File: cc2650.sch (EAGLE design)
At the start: 23 parts, among them IC4 CC2650MODAMOHR, J1 AMP FCI 10103594-0001LF, SW1 SPST_TACT-KMR2, SW2 SPST_TACT-KMR2, U402 TPS62237DRY

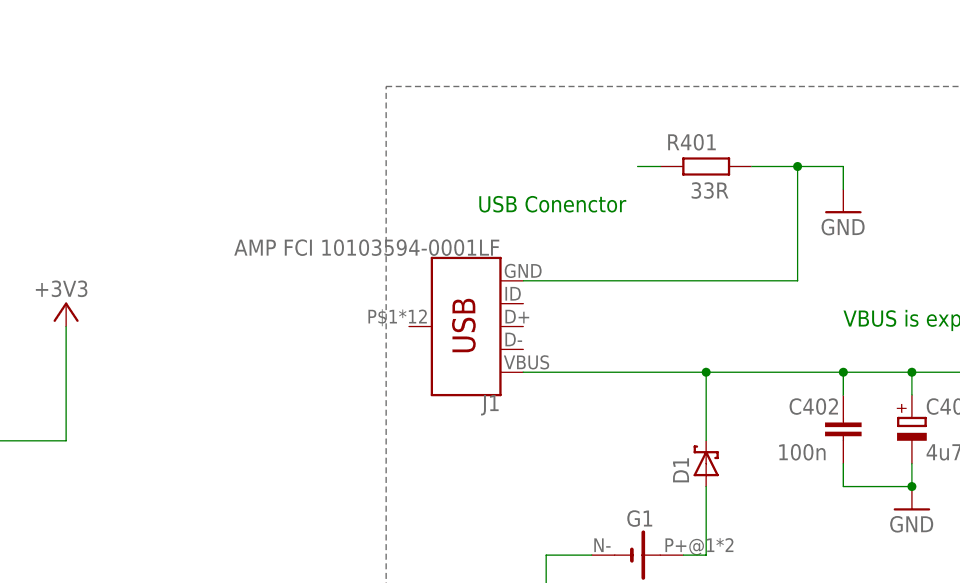
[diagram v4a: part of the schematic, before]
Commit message: Changed USB connector. Fixed error.
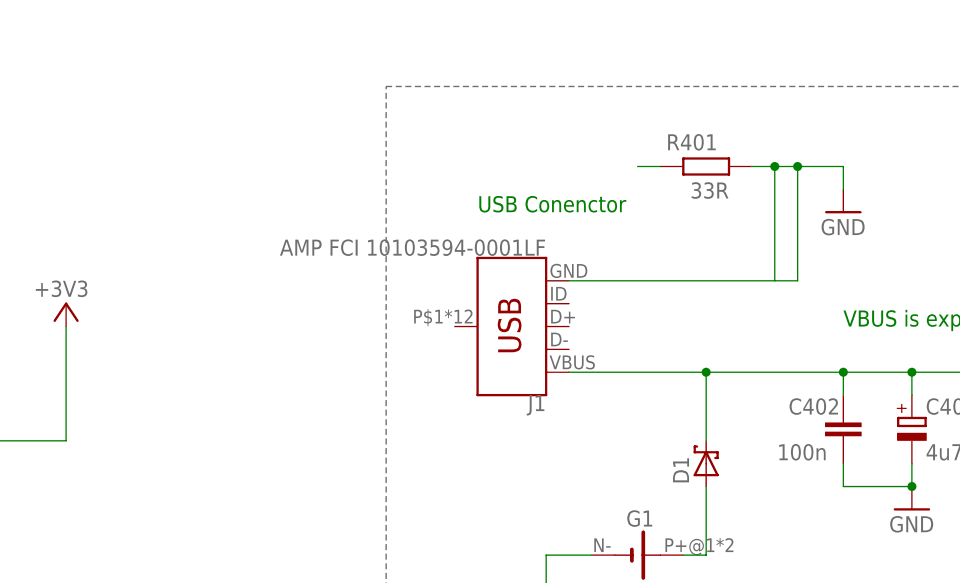
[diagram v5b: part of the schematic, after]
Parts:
- C17: MPN EVQ-Q2F03W -> (none); OC_NEWARK 96K9626 -> (none)
- C401, C402, C403, C404, D1, D2, G1, IC4, JP1, JP2, JP3, JP8, JTAG_CONNECTOR, L401, LED3, R27, R29, R401, SW1, SW2, U402: OC_NEWARK unknown -> (none)
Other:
- moved on the sheet: J1

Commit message: removed jumpers for power and leds.
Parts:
- removed JP1, JP8: LED1_PWR, jumper:JP1E
- U402: value TPS62237DRY -> TPS62233DRY
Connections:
- removed net N$7: JP8.2, R29.1
- new net PWR_LED_JMPR: JP3.4, R29.1
- net +3V3: now also JP3.2, JP3.3; no longer JP1.2, JP8.1
- net EZFET_VCC: now also JP3.1; no longer JP1.1
- net N$10: now also J1.SHIELD
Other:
- note added: "Use jumper on pins 1 & 2 for operation. Remove jumper to measure current."
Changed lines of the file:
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@@
 <part name="R29" library="rcl" deviceset="R-EU_" device="R0402" value="470R"/>
 <part name="GND21" library="supply1" deviceset="GND" device=""/>
-<part name="JP8" library="jumper" deviceset="JP1E" device="" value="LED1_PWR"/>
 <part name="LED3" library="led" deviceset="LED" device="CHIP-LED0603"/>
-<part name="+3V5" library="supply1" library_urn="urn:adsk.eagle:library:371" deviceset="+3V3" device=""/>
 <part name="GND56" library="supply1" deviceset="GND" device=""/>
 <part name="GND64" library="supply1" deviceset="GND" device=""/>
@@
 <part name="R401" library="rcl" deviceset="R-EU_" device="R0402" value="33R"/>
 <part name="C403" library="rcl" deviceset="CPOL-EU" device="A/3216-18R" value="4u7"/>
-<part name="JP1" library="jumper" deviceset="JP1E" device="" value="LED1_PWR"/>
-<part name="U402" library="tps62231dry" deviceset="TPS6223X_DRY_6" device="" value="TPS62237DRY"/>
+<part name="U402" library="tps62231dry" deviceset="TPS6223X_DRY_6" device="" value="TPS62233DRY"/>
 <part name="C404" library="CAP" deviceset="CSMD0805" device="" value="1u"/>
 <part name="C401" library="CAP" deviceset="CSMD0805" device="" value="1u"/>
@@
 <part name="GND54" library="supply1" deviceset="GND" device=""/>
 <part name="L401" library="MSP-EXP430F5659" deviceset="L-NR3010" device="" value="2.2uH (NR3010T2R2M)"/>
-<part name="+3V3" library="supply1" library_urn="urn:adsk.eagle:library:371" deviceset="+3V3" device=""/>
 <part name="D1" library="adafruit" deviceset="SCHOTTKY-DIODE" device="DO35-7"/>
 <part name="GND4" library="supply1" deviceset="GND" device=""/>
@@
 <wire x1="17.78" y1="-92.71" x2="127" y2="-92.71" width="0.1524" layer="95" style="shortdash"/>
 <text x="60.96" y="-45.72" size="1.778" layer="91">GPIO Programmable</text>
+<text x="-154.94" y="66.04" size="1.778" layer="91">Use jumper on pins 1 &amp; 2 for operation. Remove jumper to measure current.</text>
 </plain>
 <instances>
@@
 <attribute name="VALUE" x="45.72" y="83.82" size="1.778" layer="96"/>
 </instance>
-<instance part="+3V2" gate="G$1" x="-134.62" y="88.9" smashed="yes">
-<attribute name="VALUE" x="-132.08" y="91.44" size="1.778" layer="96" rot="R180"/>
+<instance part="+3V2" gate="G$1" x="-129.54" y="53.34" smashed="yes">
+<attribute name="VALUE" x="-127" y="55.88" size="1.778" layer="96" rot="R180"/>
 </instance>
 <instance part="R29" gate="G$1" x="129.54" y="68.58"/>
 <instance part="GND21" gate="1" x="154.94" y="60.96"/>
-<instance part="JP8" gate="A" x="116.84" y="71.12" smashed="yes">
-<attribute name="NAME" x="115.824" y="74.422" size="1.778" layer="95"/>
-</instance>
 <instance part="LED3" gate="G$1" x="139.7" y="68.58" rot="R90"/>
-<instance part="+3V5" gate="G$1" x="104.14" y="76.2" smashed="yes">
-<attribute name="VALUE" x="106.68" y="78.74" size="1.778" layer="96" rot="R180"/>
-</instance>
 <instance part="GND56" gate="1" x="68.58" y="17.78"/>
 <instance part="GND64" gate="1" x="76.2" y="-15.24"/>
@@
 <attribute name="NAME" x="77.724" y="-4.699" size="1.778" layer="95"/>
 <attribute name="VALUE" x="77.724" y="-9.779" size="1.778" layer="96"/>
-</instance>
-<instance part="JP1" gate="A" x="203.2" y="-7.62" smashed="yes">
-<attribute name="NAME" x="202.184" y="-4.318" size="1.778" layer="95"/>
 </instance>
 <instance part="U402" gate="&gt;NAME" x="142.24" y="-10.16"/>
@@
 <attribute name="NAME" x="160.02" y="8.89" size="1.778" layer="95" rot="R180"/>
 <attribute name="VALUE" x="170.18" y="3.81" size="1.778" layer="95" rot="R180"/>
-</instance>
-<instance part="+3V3" gate="G$1" x="213.36" y="0" smashed="yes">
-<attribute name="VALUE" x="215.9" y="2.54" size="1.778" layer="96" rot="R180"/>
 </instance>
 <instance part="D1" gate="G$1" x="53.34" y="-10.16" rot="R90"/>
@@
 <segment>
 <pinref part="+3V2" gate="G$1" pin="+3V3"/>
-<wire x1="-134.62" y1="83.82" x2="-134.62" y2="86.36" width="0.1524" layer="91"/>
-</segment>
-<segment>
-<pinref part="JP8" gate="A" pin="1"/>
-<wire x1="116.84" y1="68.58" x2="104.14" y2="68.58" width="0.1524" layer="91"/>
-<pinref part="+3V5" gate="G$1" pin="+3V3"/>
-<wire x1="104.14" y1="73.66" x2="104.14" y2="68.58" width="0.1524" layer="91"/>
-</segment>
-<segment>
-<pinref part="+3V3" gate="G$1" pin="+3V3"/>
-<wire x1="213.36" y1="-10.16" x2="213.36" y2="-2.54" width="0.1524" layer="91"/>
-<wire x1="205.74" y1="-10.16" x2="213.36" y2="-10.16" width="0.1524" layer="91"/>
-<pinref part="JP1" gate="A" pin="2"/>
+<wire x1="-129.54" y1="48.26" x2="-129.54" y2="50.8" width="0.1524" layer="91"/>
+<pinref part="JP3" gate="G$1" pin="2"/>
+<wire x1="-93.98" y1="48.26" x2="-101.6" y2="48.26" width="0.1524" layer="91"/>
+<label x="-119.38" y="48.26" size="1.778" layer="95"/>
+<pinref part="JP3" gate="G$1" pin="3"/>
+<wire x1="-101.6" y1="48.26" x2="-129.54" y2="48.26" width="0.1524" layer="91"/>
+<wire x1="-93.98" y1="45.72" x2="-101.6" y2="45.72" width="0.1524" layer="91"/>
+<wire x1="-101.6" y1="45.72" x2="-101.6" y2="48.26" width="0.1524" layer="91"/>
+<junction x="-101.6" y="48.26"/>
 </segment>
 <segment>
@@
 </segment>
 </net>
-<net name="N$7" class="0">
-<segment>
-<pinref part="JP8" gate="A" pin="2"/>
-<pinref part="R29" gate="G$1" pin="1"/>
-<wire x1="119.38" y1="68.58" x2="124.46" y2="68.58" width="0.1524" layer="91"/>
-</segment>
-</net>
 <net name="N$10" class="0">
 <segment>
-<wire x1="48.26" y1="22.86" x2="45.72" y2="22.86" width="0.1524" layer="91"/>
 <pinref part="R401" gate="G$1" pin="1"/>
+<wire x1="48.26" y1="22.86" x2="20.32" y2="22.86" width="0.1524" layer="91"/>
+<wire x1="20.32" y1="22.86" x2="20.32" y2="5.08" width="0.1524" layer="91"/>
+<pinref part="J1" gate="G$1" pin="SHIELD"/>
+<wire x1="20.32" y1="5.08" x2="25.4" y2="5.08" width="0.1524" layer="91"/>
 </segment>
 </net>
@@
 <wire x1="175.26" y1="5.08" x2="175.26" y2="-10.16" width="0.1524" layer="91"/>
 <junction x="175.26" y="-10.16"/>
-<pinref part="JP1" gate="A" pin="1"/>
+</segment>
+<segment>
+<pinref part="JP3" gate="G$1" pin="1"/>
+<wire x1="-93.98" y1="50.8" x2="-121.92" y2="50.8" width="0.1524" layer="91"/>
+<label x="-119.38" y="50.8" size="1.778" layer="95"/>
 </segment>
 </net>
@@
 </segment>
 </net>
+<net name="PWR_LED_JMPR" class="0">
+<segment>
+<pinref part="JP3" gate="G$1" pin="4"/>
+<wire x1="-93.98" y1="43.18" x2="-121.92" y2="43.18" width="0.1524" layer="91"/>
+<label x="-119.38" y="43.18" size="1.778" layer="95"/>
+</segment>
+<segment>
+<pinref part="R29" gate="G$1" pin="1"/>
+<wire x1="124.46" y1="68.58" x2="101.6" y2="68.58" width="0.1524" layer="91"/>
+<label x="104.14" y="68.58" size="1.778" layer="95"/>
+</segment>
+</net>

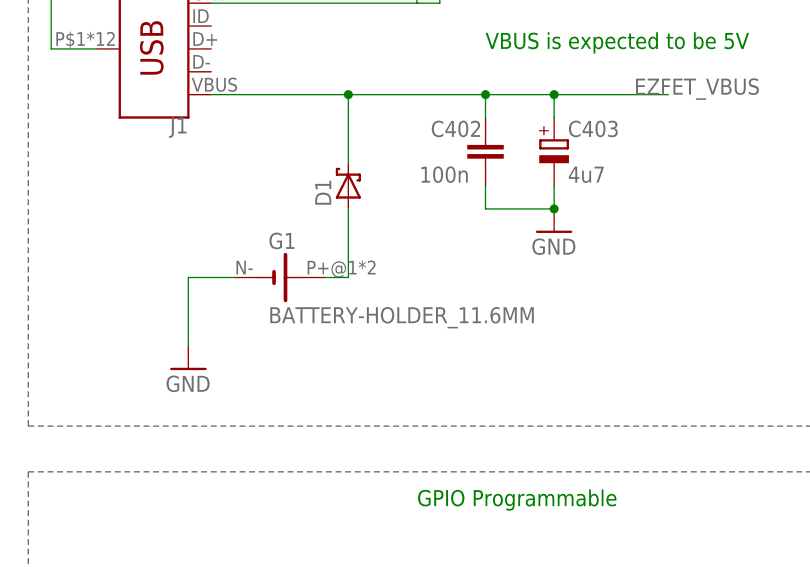
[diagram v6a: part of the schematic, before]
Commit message: changed out battery to cc1220.
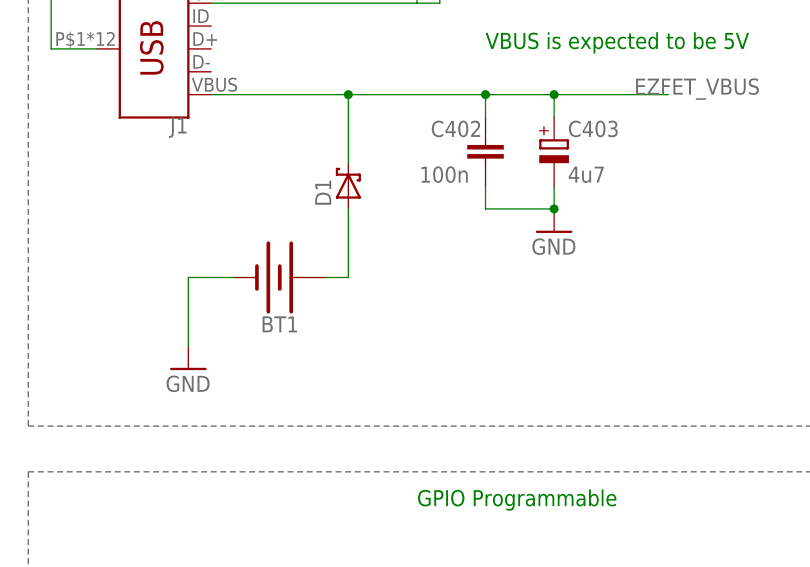
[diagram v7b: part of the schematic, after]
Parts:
- removed G1: BATTERY-HOLDER_11.6MM, battery:BATTERY-HOLDER_11.6MM
- added BT1: (no value), SparkFun-Batteries:BATTERY-12MM_SMD
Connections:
- net GND: now also BT1.-; no longer G1.-
- net N$3: now also BT1.+; no longer G1.+
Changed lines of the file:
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@@
 <part name="+3V1" library="supply1" library_urn="urn:adsk.eagle:library:371" deviceset="+3V3" device=""/>
 <part name="GND2" library="supply1" library_urn="urn:adsk.eagle:library:371" deviceset="GND" device=""/>
-<part name="G1" library="battery" library_urn="urn:adsk.eagle:library:109" deviceset="BATTERY-HOLDER_11.6MM" device="" package3d_urn="urn:adsk.eagle:package:4616/1"/>
 <part name="SW1" library="adafruit" deviceset="SPST_TACT" device="-KMR2"/>
 <part name="SW2" library="adafruit" deviceset="SPST_TACT" device="-KMR2"/>
@@
 <part name="+3V7" library="supply1" library_urn="urn:adsk.eagle:library:371" deviceset="+3V3" device=""/>
 <part name="J1" library="SparkFun-Connectors" deviceset="USB_MICRO-B" device="_HALF_PTH" value="AMP FCI 10103594-0001LF"/>
+<part name="BT1" library="SparkFun-Batteries" deviceset="BATTERY" device="-12MM_SMD"/>
 </parts>
 <sheets>
@@
 </instance>
 <instance part="GND2" gate="1" x="-106.68" y="-48.26"/>
-<instance part="G1" gate="G$1" x="45.72" y="-20.32"/>
 <instance part="SW1" gate="G$1" x="55.88" y="60.96"/>
 <instance part="SW2" gate="G$1" x="45.72" y="-73.66" rot="R90"/>
@@
 </instance>
 <instance part="J1" gate="G$1" x="33.02" y="5.08" rot="R180"/>
+<instance part="BT1" gate="G$1" x="45.72" y="-20.32" rot="R180"/>
 </instances>
 <busses>
@@
 </segment>
 <segment>
-<pinref part="G1" gate="G$1" pin="-"/>
-<wire x1="40.64" y1="-20.32" x2="35.56" y2="-20.32" width="0.1524" layer="91"/>
 <wire x1="35.56" y1="-20.32" x2="35.56" y2="-27.94" width="0.1524" layer="91"/>
 <pinref part="GND4" gate="1" pin="GND"/>
+<pinref part="BT1" gate="G$1" pin="-"/>
+<wire x1="40.64" y1="-20.32" x2="35.56" y2="-20.32" width="0.1524" layer="91"/>
 </segment>
 <segment>
@@
 <pinref part="D1" gate="G$1" pin="A"/>
 <wire x1="53.34" y1="-12.7" x2="53.34" y2="-20.32" width="0.1524" layer="91"/>
-<pinref part="G1" gate="G$1" pin="+"/>
-<wire x1="53.34" y1="-20.32" x2="50.8" y2="-20.32" width="0.1524" layer="91"/>
+<pinref part="BT1" gate="G$1" pin="+"/>
+<wire x1="50.8" y1="-20.32" x2="53.34" y2="-20.32" width="0.1524" layer="91"/>
 </segment>
 </net>
@@
 will not be understood (or retained) with this version.
 </note>
-<note version="8.3" severity="warning">
-Since Version 8.3, EAGLE supports the association of 3D packages
-with devices in libraries, schematics, and board files. Those 3D
-packages will not be understood (or retained) with this version.
-</note>
 </compatibility>

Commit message: Added GND planes. Replaced some schematic symbols w/ US ones.
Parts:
- removed C17: 1n, rcl:C-EUC0402
- removed C401, C404: 1u, CAP:CSMD0805
- removed C402: 100n, rcl:C-EUC0402
- removed C403: 4u7, rcl:CPOL-EUA/3216-18R
- removed R27: 47k, rcl:R-EU_R0402
- removed R29: 470R, rcl:R-EU_R0402
- removed R401: 33R, rcl:R-EU_R0402
- added C1: 100n, adafruit:C-USC0402
- added C2: 4u7, adafruit:C-USC1206
- added C3, C4: 1u, adafruit:C-USC0805
- added C5: 1n, adafruit:C-USC0402
- added R1: 47k, adafruit:R-US_R0402
- added R2: 470, adafruit:R-US_R0402
- added R3: 33, adafruit:R-US_R0402
- added U$1: (no value), adafruit:CR1220THM
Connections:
- removed net +3V3: IC4.VDD(1), IC4.VDD(2), JP2.15, JP3.2, JP3.3, JTAG_CONNECTOR.1, R27.2
- new net VCC: IC4.VDD(1), IC4.VDD(2), JP2.15, JP3.2, JP3.3, JTAG_CONNECTOR.1, R1.1
- net EZFET_VBUS: now also C1.1, C2.1, C3.1; no longer C402.1, C403.+, C404.2
- net EZFET_VCC: now also C4.1; no longer C401.2
- net GND: now also C1.2, C2.2, C3.2, C4.2, C5.2, R3.2, SW1.P; no longer C17.2, C401.1, C402.2, C403.-, C404.1, R401.2
- net N$10: now also R3.1; no longer R401.1
- net N$32: now also R2.2; no longer R29.2
- net NRESET: now also C5.1, R1.2; no longer C17.1, R27.1
- net PWR_LED_JMPR: now also R2.1; no longer R29.1
